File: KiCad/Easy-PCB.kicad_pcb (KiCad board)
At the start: 2 copper layers, 177.8 x 83.8 mm, 110 parts, among them J1 703W-00/53, J3 HLW20R-2C7LF, K1 G5LE-1A-E_DC12, P1 1x02, P10 via, P11 via, P12 M20-9980346, P13 via, P14 via, P15 via, P16 via, P17 via, P18 via, P19 via, P2 1x06, P24 M20-9980346, P3 1x04, P4 1x03 Terminal Block, P5 1x02, P6 via, P7 via, P8 via, P9 via, Q1 2N3904, Q10 MJE350, Q11 2N3904, Q12 2N3904, Q13 MJE340, Q14 MJE350, Q15 2N3904, Q16 MJE340, Q17 MJE350, Q18 2N3904, Q19 2N3904, Q2 MJE340, Q3 2N3904, Q4 2N3904, Q5 MJE340, Q6 MJE350, Q7 2N3904, Q8 2N3904, Q9 MJE340, SW1 R1966ABLKBLKFR, T1 VPP24-830, U1 PIC16F883, U2 MCP41050, U3 MCP617, U4 MCP9700A, U5 LM7805

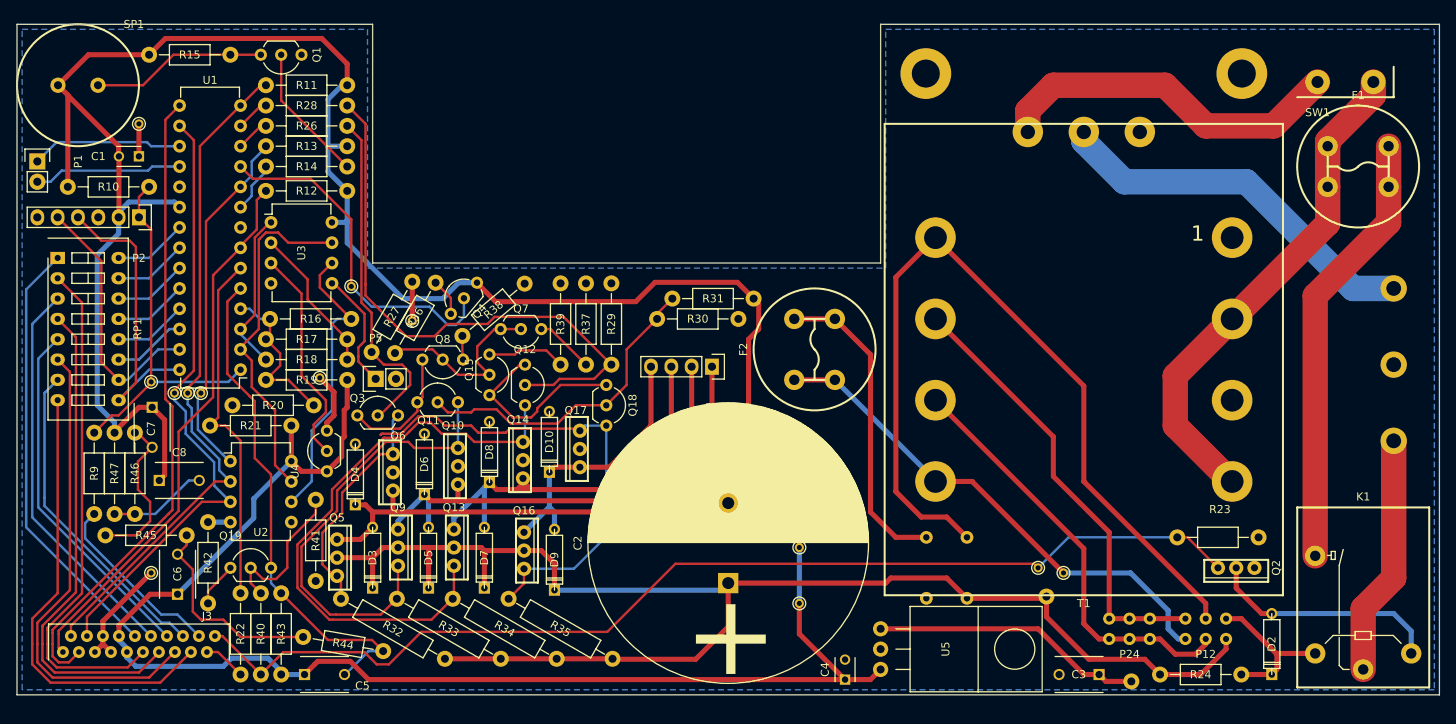
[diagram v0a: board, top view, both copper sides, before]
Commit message: added mounting cutouts to driver board
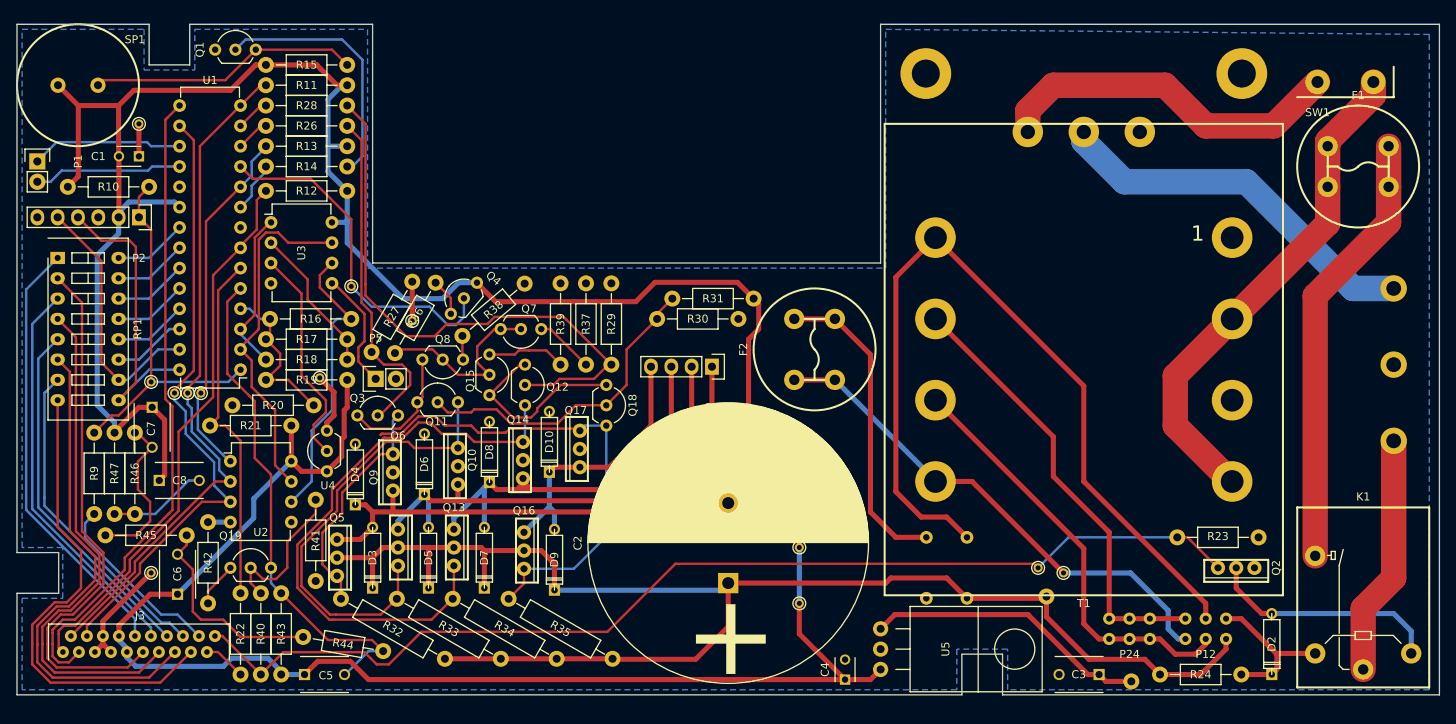
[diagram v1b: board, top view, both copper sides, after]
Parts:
- added P22: Screw Mounting, Easy-PCB-footprints:10-32, F.Cu at (53.3, 106.3)
- moved R15 14.7 mm to (87.0, 43.2)
- moved Q1 10.8 mm to (75.6, 41.3), turned to 0 degrees
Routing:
- net Net-(Q1-Pad2): track 17.4 -> 31.9 mm
- net Net-(Q1-Pad3): track 21.9 -> 33.8 mm
- net VDD: track 423.2 -> 414.7 mm
- net Net-(J3-Pad15): track 59.5 -> 63.1 mm
- net Net-(J3-Pad13): track 61.6 -> 65.0 mm
- net Net-(J3-Pad17): track 56.7 -> 60.0 mm
- net Net-(J3-Pad11): track 63.8 -> 66.9 mm
- net VDDunreg: track 34.1 -> 35.5 mm
- net MISO: track 80.3 -> 81.2 mm
- net CS1: track 68.6 -> 69.4 mm
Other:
- outline, holes or cut-outs redrawn
- board text added: "Cutouts for 10-32 Mouting Screws"
